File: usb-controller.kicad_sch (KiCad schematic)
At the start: 39 parts, among them U1501 UPD720201K8-701-BAC-A, U1502 W25Q80DV_USON, Y1501 Resonator_24MHz_ECX-1247

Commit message: [#100282] WIP: Clear ERC
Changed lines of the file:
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@@
 	)
 	(junction
+		(at 276.86 101.6)
+		(diameter 0)
+		(color 0 0 0 0)
+	)
+	(junction
+		(at 284.48 101.6)
+		(diameter 0)
+		(color 0 0 0 0)
+	)
+	(junction
 		(at 308.61 101.6)
 		(diameter 0)
@@
 	(wire
 		(pts
+			(xy 276.86 101.6) (xy 284.48 101.6)
+		)
+		(stroke
+			(width 0)
+			(type default)
+		)
+	)
+	(wire
+		(pts
 			(xy 254 127) (xy 254 130.81)
 		)
@@
 	(wire
 		(pts
-			(xy 241.3 101.6) (xy 241.3 102.87)
+			(xy 243.84 101.6) (xy 243.84 102.87)
 		)
 		(stroke
@@
 	(wire
 		(pts
+			(xy 284.48 100.33) (xy 284.48 101.6)
+		)
+		(stroke
+			(width 0)
+			(type default)
+		)
+	)
+	(wire
+		(pts
 			(xy 238.76 204.47) (xy 241.3 204.47)
 		)
@@
 	(wire
 		(pts
+			(xy 284.48 101.6) (xy 288.29 101.6)
+		)
+		(stroke
+			(width 0)
+			(type default)
+		)
+	)
+	(wire
+		(pts
 			(xy 238.76 123.19) (xy 254 123.19)
 		)
@@
 	(wire
 		(pts
+			(xy 276.86 100.33) (xy 276.86 101.6)
+		)
+		(stroke
+			(width 0)
+			(type default)
+		)
+	)
+	(wire
+		(pts
 			(xy 308.61 85.09) (xy 308.61 86.36)
 		)
@@
 	(wire
 		(pts
+			(xy 243.84 102.87) (xy 241.3 102.87)
+		)
+		(stroke
+			(width 0)
+			(type default)
+		)
+	)
+	(wire
+		(pts
 			(xy 288.29 109.22) (xy 288.29 107.95)
 		)
@@
 	(wire
 		(pts
-			(xy 241.3 101.6) (xy 288.29 101.6)
+			(xy 243.84 101.6) (xy 276.86 101.6)
 		)
 		(stroke
@@
 		(length 2.54)
 		(shape round)
+		(at 276.86 100.33 0)
+		(effects
+			(font
+				(size 1.27 1.27)
+			)
+			(justify left bottom)
+		)
+		(property "Net Class" "PWR"
+			(at 275.59 97.79 0)
+			(show_name no)
+			(do_not_autoplace no)
+			(effects
+				(font
+					(size 1.27 1.27)
+				)
+				(justify right)
+			)
+		)
+		(property "Component Class" ""
+			(at 554.99 215.9 0)
+			(show_name no)
+			(do_not_autoplace no)
+			(effects
+				(font
+					(size 1.27 1.27)
+					(italic yes)
+				)
+			)
+		)
+	)
+	(netclass_flag ""
+		(length 2.54)
+		(shape round)
 		(at 149.86 170.18 180)
 		(fields_autoplaced yes)
@@
 					(unit 1)
 				)
+			)
+		)
+	)
+	(symbol
+		(lib_id "antmicropower:PWR_FLAG")
+		(at 284.48 100.33 0)
+		(unit 1)
+		(body_style 1)
+		(exclude_from_sim no)
+		(in_bom yes)
+		(on_board yes)
+		(in_pos_files yes)
+		(dnp no)
+		(property "Reference" "#FLG01501"
+			(at 284.48 98.425 0)
+			(hide yes)
+			(show_name no)
+			(do_not_autoplace no)
+			(effects
+				(font
+					(size 1.27 1.27)
+				)
+			)
+		)
+		(property "Value" "PWR_FLAG"
+			(at 284.48 96.52 0)
+			(show_name no)
+			(do_not_autoplace no)
+			(effects
+				(font
+					(size 1.27 1.27)
+				)
+			)
+		)
+		(property "Footprint" ""
+			(at 284.48 100.33 0)
+			(hide yes)
+			(show_name no)
+			(do_not_autoplace no)
+			(effects
+				(font
+					(size 1.27 1.27)
+				)
+			)
+		)
+		(property "Datasheet" ""
+			(at 284.48 100.33 0)
+			(hide yes)
+			(show_name no)
+			(do_not_autoplace no)
+			(effects
+				(font
+					(size 1.27 1.27)
+				)
+			)
+		)
+		(property "Description" ""
+			(at 284.48 102.87 0)
+			(hide yes)
+			(show_name no)
+			(do_not_autoplace no)
+			(effects
+				(font
+					(size 1.27 1.27)
+				)
+				(justify left bottom)
+			)
+		)
+		(pin "1"
+		)
+		(instances
+			(project "altera-modular-agilex-5-dc-scm"
+				(path "/6bb9d978-a328-4b30-874b-55170a976185/438e9c44-46ce-4859-a53d-b917b2709c50"
+					(reference "#FLG01501")
+					(unit 1)
+				)

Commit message: [#100282] Update components from library
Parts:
- U1501: footprint antmicro-footprints:UPD720201K8-701-BAC-A -> antmicro-footprints:QFN-68-1EP_8x8mm_P0.4mm
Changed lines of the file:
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@@
 			)
 		)
-		(property "Description" "SMD Chip Resistor"
+		(property "Description" "SMD Chip Resistor, 1.6 kohm, ± 1%, 62.5 mW, 0402 [1005 Metric], Thick Film, General Purpose"
 			(at 265.43 229.87 0)
 			(hide yes)
@@
 			)
 		)
-		(property "Footprint" "antmicro-footprints:UPD720201K8-701-BAC-A"
+		(property "Footprint" "antmicro-footprints:QFN-68-1EP_8x8mm_P0.4mm"
 			(at 254 107.95 0)
 			(hide yes)

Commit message: [#100282] Clear ERC
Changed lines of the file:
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@@
 		)
 	)
+	(wire
+		(pts
+			(xy 180.34 97.79) (xy 190.5 97.79)
+		)
+		(stroke
+			(width 0)
+			(type default)
+		)
+	)
 	(bus
 		(pts
@@
 	(wire
 		(pts
-			(xy 190.5 97.79) (xy 180.34 97.79)
-		)
-		(stroke
-			(width 0)
-			(type default)
-		)
-	)
-	(wire
-		(pts
 			(xy 170.18 97.79) (xy 170.18 99.06)
 		)
@@
 		(in_pos_files yes)
 		(dnp no)
-		(fields_autoplaced yes)
 		(property "Reference" "#PWR01503"
 			(at 130.81 100.33 0)
@@
 		)
 		(property "Value" "+3.3V"
-			(at 130.81 91.44 0)
+			(at 130.81 92.71 0)
 			(show_name no)
 			(do_not_autoplace no)

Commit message: [#100282] Fix overlaping graphics, add schematic sheet names on them
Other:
- note added: "USB controller"
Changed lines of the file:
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@@
+		)
+	)
+	(text "USB controller"
+		(exclude_from_sim no)
+		(at 203.2 38.1 0)
+		(effects
+			(font
+				(size 4 4)
+				(thickness 0.8)
+				(bold yes)
+			)
 		)
 	)

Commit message: [#99852] Add PONRST control to USB controller
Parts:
- removed FB1501: FB_30Z_3.1A_Murata-BLM15KD300SN1D_0402, antmicro-footprints:FB_0402_1005Metric, symbol antmicroFerriteBeadsandChips:FB_30Z_3.1A_Murata-BLM15KD300SN1D_0402
- added C1525: C_100n_0402, antmicro-footprints:C_0402_1005Metric, symbol antmicroCapacitors0402:C_100n_0402
- added FB1501: FB_60Z_3.5A_Murata-BLM21PG_0805, antmicro-footprints:FB_0805_2012Metric, symbol antmicroFerriteBeadsandChips:FB_60Z_3.5A_Murata-BLM21PG_0805
- added Q1501: 2N7002PV, antmicro-footprints:SOT-563, symbol antmicroTransistorsFETsMOSFETsArrays:2N7002PV
- added R1509: R_0R_0402, antmicro-footprints:R_0402_1005Metric, symbol antmicroResistors0402:R_0R_0402
- added R1510, R1511: R_1k_0402, antmicro-footprints:R_0402_1005Metric, symbol antmicroResistors0402:R_1k_0402
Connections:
- net +3.3V: now also FB1501.2, R1510.2
- net GND: now also C1525.1, Q1501.1 (S1), Q1501.4 (S2), R1511.1
- net ~{USBCTRL_POR}: now also Q1501.6 (D1), R1511.2
- net at C1518.2, C1519.2, C1520.2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: now also FB1501.1
- new net: Q1501.3 (D2), R1509.1, R1510.1
- new net: C1525.2, Q1501.2 (G1), R1509.2
- new net 1V05_PG: Q1501.5 (G2)
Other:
- note removed: "TODO: Ref design used BLM21PG600SN1"
- note removed: "TODO: Swap RC with Power sequencing IC"
- note removed: "USB controller"
- moved on the sheet: TP1501

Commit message: [#99852] Pull down unused USB 3.0 RX lines
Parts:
- added R1512, R1513: R_1k6_0402, antmicro-footprints:R_0402_1005Metric, symbol antmicroResistors0402:R_1k6_0402
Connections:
- net GND: now also R1512.1, R1513.1
- net USBSS3.RX+: now also R1513.2
- net USBSS3.RX-: now also R1512.2
- no-connect marks 0 -> 6

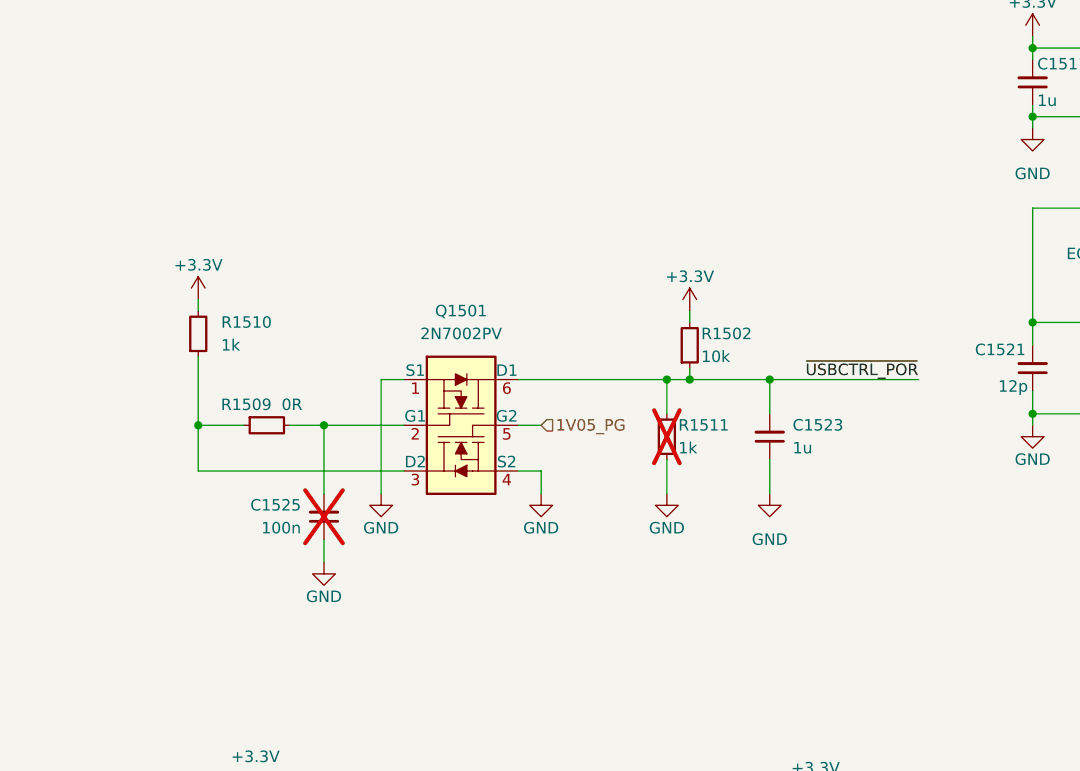
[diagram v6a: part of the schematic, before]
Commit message: [#100282] Use single instead of dual transistors to control USBCTRL_POR signal
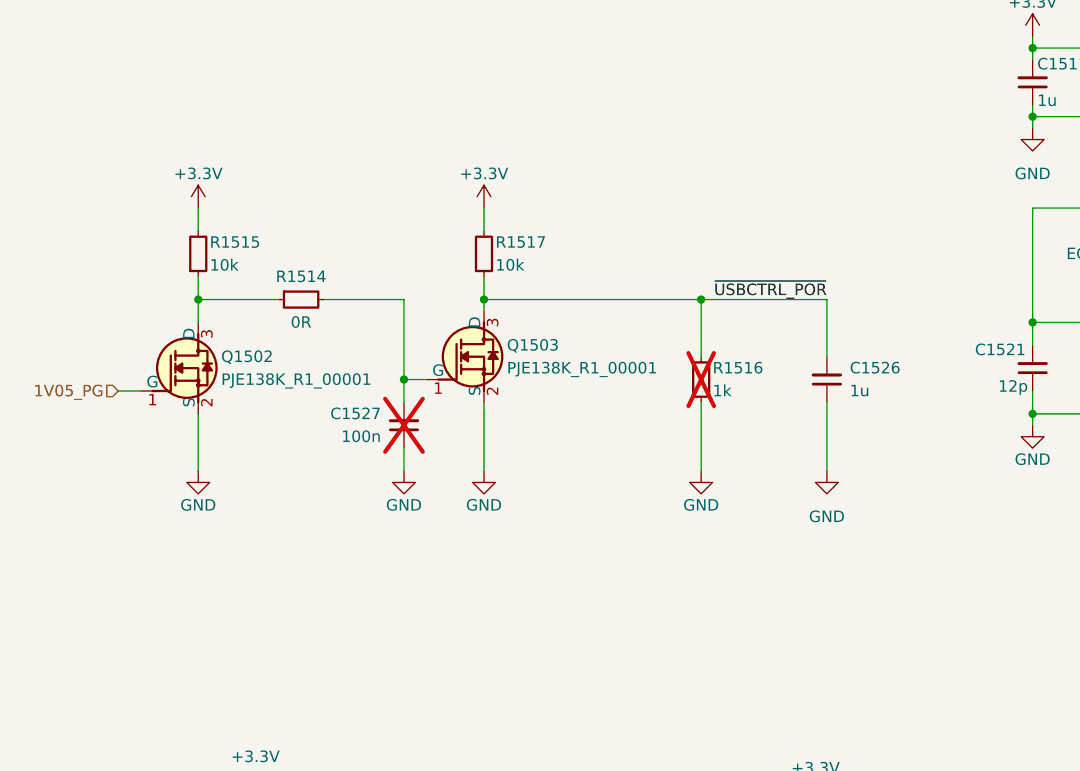
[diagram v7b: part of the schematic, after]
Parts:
- removed C1523: C_1u_10V_X7R_0402, antmicro-footprints:C_0402_1005Metric, symbol antmicroCapacitors0402:C_1u_10V_X7R_0402
- removed C1525: C_100n_0402, antmicro-footprints:C_0402_1005Metric, symbol antmicroCapacitors0402:C_100n_0402
- removed Q1501: 2N7002PV, antmicro-footprints:SOT-563, symbol antmicroTransistorsFETsMOSFETsArrays:2N7002PV
- removed R1502: R_10k_0402, antmicro-footprints:R_0402_1005Metric, symbol antmicroResistors0402:R_10k_0402
- removed R1509: R_0R_0402, antmicro-footprints:R_0402_1005Metric, symbol antmicroResistors0402:R_0R_0402
- removed R1510, R1511: R_1k_0402, antmicro-footprints:R_0402_1005Metric, symbol antmicroResistors0402:R_1k_0402
- added C1526: C_1u_10V_X7R_0402, antmicro-footprints:C_0402_1005Metric, symbol antmicroCapacitors0402:C_1u_10V_X7R_0402
- added C1527: C_100n_0402, antmicro-footprints:C_0402_1005Metric, symbol antmicroCapacitors0402:C_100n_0402
- added Q1502, Q1503: PJE138K, antmicro-footprints:SOT-523, symbol antmicroTransistorsFETsMOSFETsSingle:PJE138K
- added R1514: R_0R_0402, antmicro-footprints:R_0402_1005Metric, symbol antmicroResistors0402:R_0R_0402
- added R1515, R1517: R_10k_0402, antmicro-footprints:R_0402_1005Metric, symbol antmicroResistors0402:R_10k_0402
- added R1516: R_1k_0402, antmicro-footprints:R_0402_1005Metric, symbol antmicroResistors0402:R_1k_0402
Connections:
- net +3.3V: now also R1515.2, R1517.2
- net 1V05_PG: now also Q1502.1 (G)
- net GND: now also C1526.1, C1527.1, Q1502.2 (S), Q1503.2 (S), R1516.1
- net ~{USBCTRL_POR}: now also C1526.2, Q1503.3 (D), R1516.2, R1517.1
- new net: C1527.2, Q1503.1 (G), R1514.2
- new net: Q1502.3 (D), R1514.1, R1515.1
